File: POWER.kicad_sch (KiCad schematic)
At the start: 9 parts

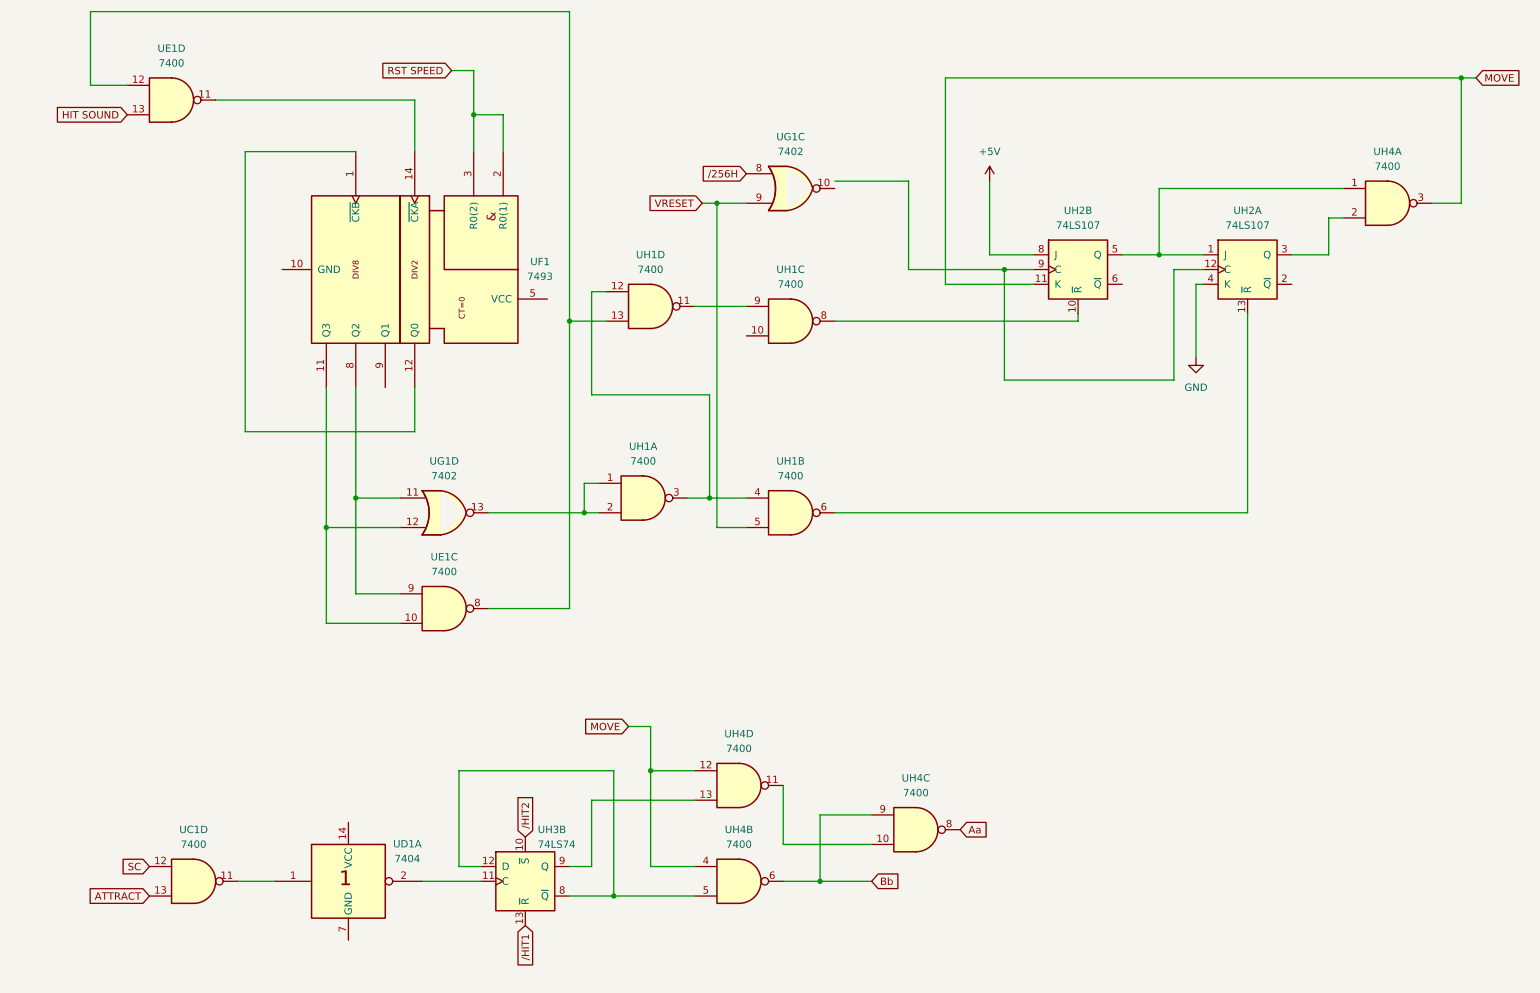
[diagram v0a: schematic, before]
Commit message: Added remainder of sheets
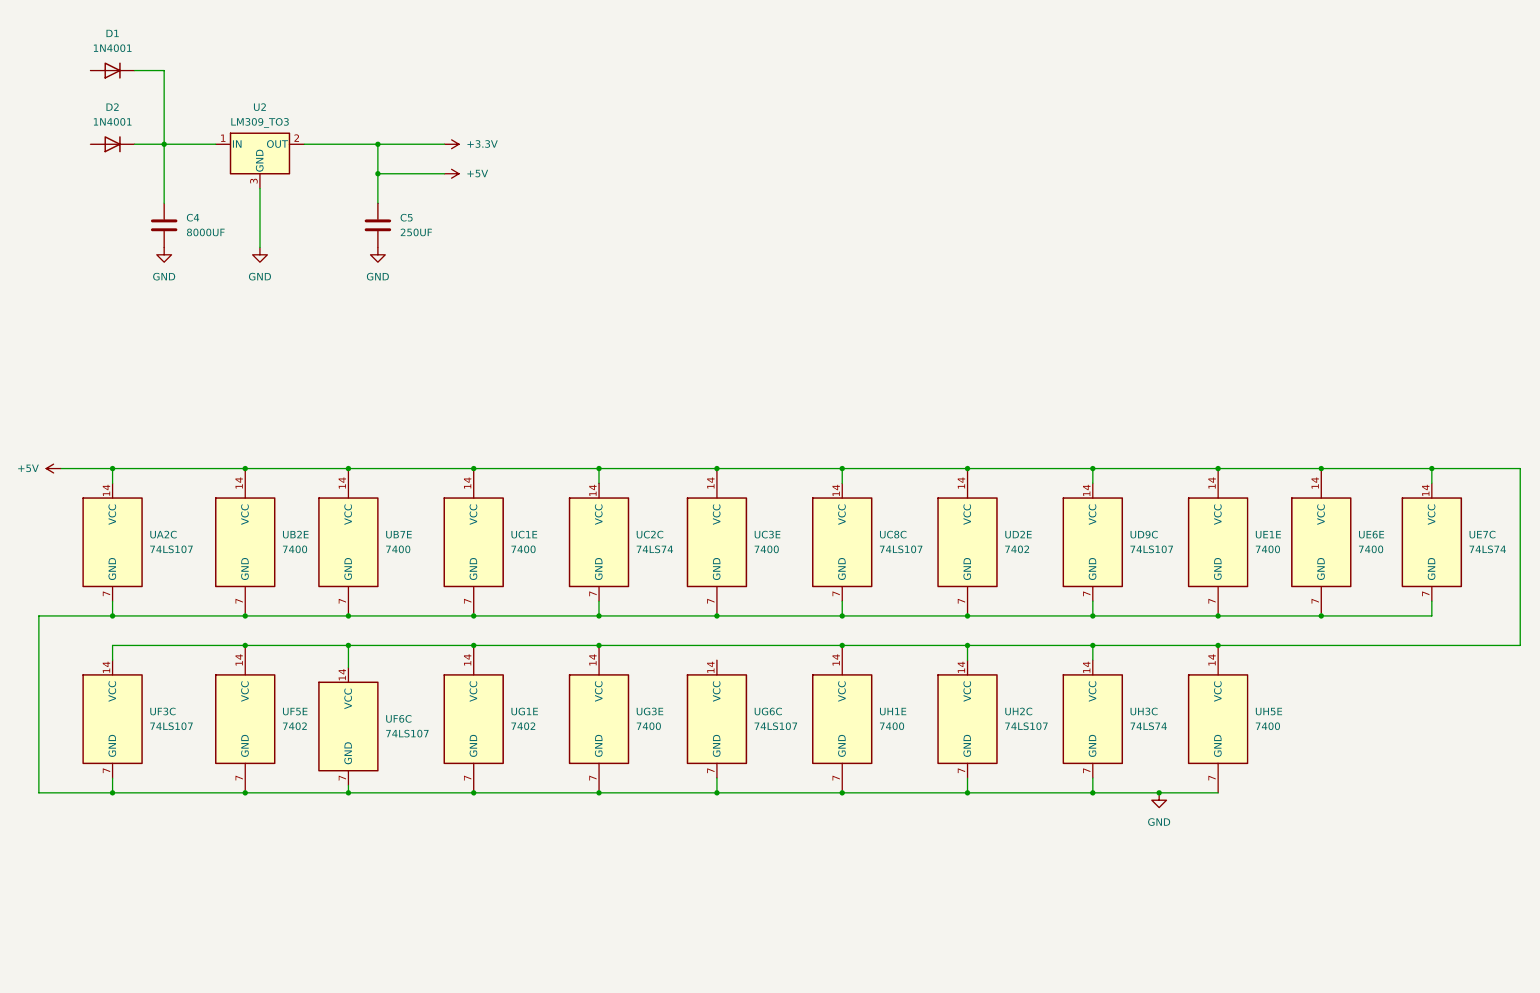
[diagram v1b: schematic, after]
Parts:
- removed UC1, UE1, UH1, UH4: 7400, Package_DIP:DIP-14_W7.62mm_Socket_LongPads, symbol 74xx:7400
- removed UD1: 7404, Package_DIP:DIP-14_W7.62mm_Socket_LongPads, symbol 74xx_IEEE:7404
- removed UF1: 7493, Package_DIP:DIP-14_W7.62mm_Socket_LongPads, symbol 74xx_IEEE:7493
- removed UG1: 7402, Package_DIP:DIP-14_W7.62mm_Socket_LongPads, symbol 74xx:7402
- removed UH2: 74LS107, Package_DIP:DIP-14_W7.62mm_Socket_LongPads, symbol 74xx:74LS107
- removed UH3: 74LS74, Package_DIP:DIP-14_W7.62mm_Socket_LongPads, symbol 74xx:74LS74
- added C4: 8000UF, symbol Device:C
- added C5: 250UF, symbol Device:C
- added D1, D2: 1N4001, Diode_THT:D_DO-41_SOD81_P10.16mm_Horizontal, symbol Diode:1N4001
- added U2: LM309_TO3, Package_TO_SOT_THT:TO-3, symbol pong:LM309_TO3
- added UA2, UC8, UD9, UF3, UF6, UG6, UH2: 74LS107, Package_DIP:DIP-14_W7.62mm_Socket_LongPads, symbol 74xx:74LS107
- added UB2, UB7, UC1, UC3, UE1, UE6, UG3, UH1, UH5: 7400, Package_DIP:DIP-14_W7.62mm_Socket_LongPads, symbol 74xx:7400
- added UC2, UE7, UH3: 74LS74, Package_DIP:DIP-14_W7.62mm_Socket_LongPads, symbol 74xx:74LS74
- added UD2, UF5, UG1: 7402, Package_DIP:DIP-14_W7.62mm_Socket_LongPads, symbol 74xx:7402
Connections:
- net GND: now also C4.2, C5.2, U2.3 (GND), UA2.7 (GND), UB2.7 (GND), UB7.7 (GND), UC1.7 (GND), UC2.7 (GND), UC3.7 (GND), UC8.7 (GND), UD2.7 (GND), UD9.7 (GND), UE1.7 (GND), UE6.7 (GND), UE7.7 (GND), UF3.7 (GND), UF5.7 (GND), UF6.7 (GND), UG1.7 (GND), UG3.7 (GND), UG6.7 (GND), UH1.7 (GND), UH2.7 (GND), UH3.7 (GND), UH5.7 (GND)
- new net: C4.1, D1.1 (K), D2.1 (K), U2.1 (IN)
- new net +3.3V: C5.1, U2.2 (OUT), UA2.14 (VCC), UB2.14 (VCC), UB7.14 (VCC), UC1.14 (VCC), UC2.14 (VCC), UC3.14 (VCC), UC8.14 (VCC), UD2.14 (VCC), UD9.14 (VCC), UE1.14 (VCC), UE6.14 (VCC), UE7.14 (VCC), UF3.14 (VCC), UF5.14 (VCC), UF6.14 (VCC), UG1.14 (VCC), UG3.14 (VCC), UH1.14 (VCC), UH2.14 (VCC), UH3.14 (VCC), UH5.14 (VCC)

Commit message: R20260915
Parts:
- U2: value LM309_TO3 -> LM309
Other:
- company: (none) -> Atari
- title: (none) -> PONG
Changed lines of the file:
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@@
 	(generator_version "10.0")
 	(paper "USLetter")
+	(title_block
+		(title "PONG")
+		(company "Atari")
+	)
 	(junction
 		(at 259.08 96.52)
@@
 	)
 	(symbol
-		(lib_id "power:+3.3V")
+		(lib_id "power:VCC")
 		(at 88.9 40.64 270)
 		(unit 1)
@@
 		(dnp no)
 		(fields_autoplaced yes)
-		(property "Reference" "#PWR09"
+		(property "Reference" "#PWR9"
 			(at 85.09 40.64 0)
 			(hide yes)
@@
 			)
 		)
-		(property "Description" "Power symbol creates a global label with name \"+3.3V\""
+		(property "Description" "Power symbol creates a global label with name \"VCC\""
 			(at 88.9 40.64 0)
 			(hide yes)
@@
 			(project "pong"
 				(path "/6c55baa6-be38-444e-ac95-9cecf812b759/5b167edd-bd23-45e2-aa73-9f69e0f47c29"
-					(reference "#PWR09")
+					(reference "#PWR9")
 					(unit 1)
 				)
@@
 			)
 		)
-		(property "Value" "LM309_TO3"
+		(property "Value" "LM309"
 			(at 57.15 36.83 0)
 			(show_name no)

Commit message: R20260918
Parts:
- added UA5, UB5: 74LS74, pong:pong_DIP-14_W7.62mm_Socket_LongPads, symbol 74xx:74LS74
- UA2, UB2, UB7, UC1, UC2, UC3, UC8, UD2, UD9, UE1, UE6, UE7, UF3, UF5, UF6, UG1, UG3, UG6, UH1, UH2, UH3, UH5: footprint Package_DIP:DIP-14_W7.62mm_Socket_LongPads -> pong:pong_DIP-14_W7.62mm_Socket_LongPads

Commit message: R20260921
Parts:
- added C13, C14, C15, C16, C17, C18, C19, C20, C21: C_US, Capacitor_THT:C_Disc_D16.0mm_W5.0mm_P10.00mm, symbol Device:C_US
- added UH4: 7400, pong:pong_DIP-14_W7.62mm_Socket_LongPads, symbol 74xx:7400
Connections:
- net +3.3V: now also UA5.14 (VCC), UB5.14 (VCC), C13.1, C14.1, C15.1, C16.1, C17.1, C18.1, C19.1, C20.1, C21.1, UH4.14 (VCC)
- net GND: now also UA5.7 (GND), UB5.7 (GND), C13.2, C14.2, C15.2, C16.2, C17.2, C18.2, C19.2, C20.2, C21.2, UH4.7 (GND)
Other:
- moved on the sheet: UA5C, UB5C

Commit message: R20260922
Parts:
- C4: value 8000UF -> 8000UF 15V
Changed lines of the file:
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@@
 			)
 		)
-		(property "Value" "8000UF"
+		(property "Value" "8000UF 15V"
 			(at 44.45 55.8799 0)
 			(show_name no)
@@
 			)
 		)
-		(property "Datasheet" ""
+		(property "Datasheet" "https://www.vishay.com/docs/42036/39d.pdf"
 			(at 40.64 54.61 0)
 			(hide yes)

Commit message: R20260922PM
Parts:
- added UA6, UB6: 7450, pong:pong_DIP-14_W7.62mm_Socket_LongPads, symbol d1:7450
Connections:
- net +3.3V: now also UA6.14 (VCC), UB6.14 (VCC)
- net GND: now also UA6.7 (GND), UB6.7 (GND)

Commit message: R20260924
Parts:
- added J1: Conn_02x22_Top_Bottom, symbol Connector_Generic:Conn_02x22_Top_Bottom
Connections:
- net GND: now also J1.1 (Pin_1), J1.2 (Pin_2), J1.21 (Pin_21), J1.22 (Pin_22), J1.8 (Pin_8), J1.9 (Pin_9)
- net 6: now reaches D2.2 (A)
- net 6: now also J1.6 (Pin_6)
- net 4: now reaches D1.2 (A)
- net 4: now also J1.4 (Pin_4)
- new net 10: J1.10 (Pin_10)
- new net 11: J1.11 (Pin_11)
- new net 12: J1.12 (Pin_12)
- new net 13: J1.13 (Pin_13)
- new net 14: J1.14 (Pin_14)
- new net 15: J1.15 (Pin_15)
- new net 16: J1.16 (Pin_16)
- new net 17: J1.17 (Pin_17)
- new net 18: J1.18 (Pin_18)
- new net 19: J1.19 (Pin_19)
- new net 20: J1.20 (Pin_20)
- new net 3: J1.3 (Pin_3)
- new net 5: J1.5 (Pin_5)
- new net 7: J1.7 (Pin_7)
